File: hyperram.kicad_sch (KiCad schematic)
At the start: 7 parts, among them U2001 IS66WVH16M8DBLL-100B1LI

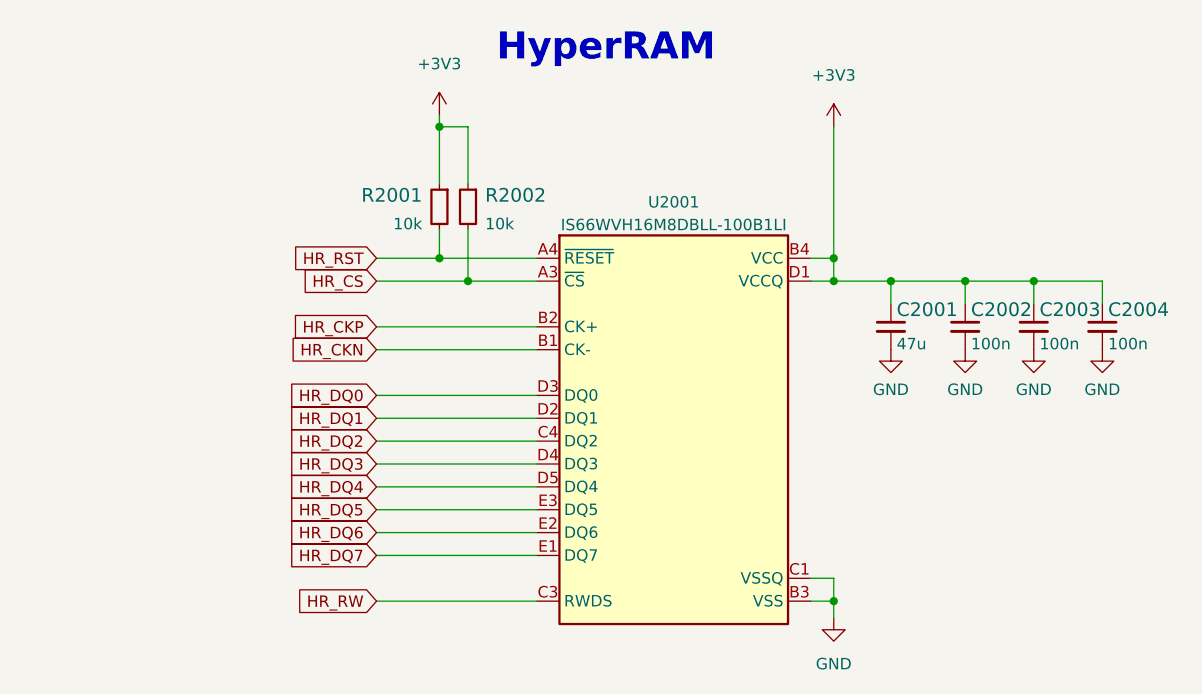
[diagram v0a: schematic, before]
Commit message: Re-annotate schematic
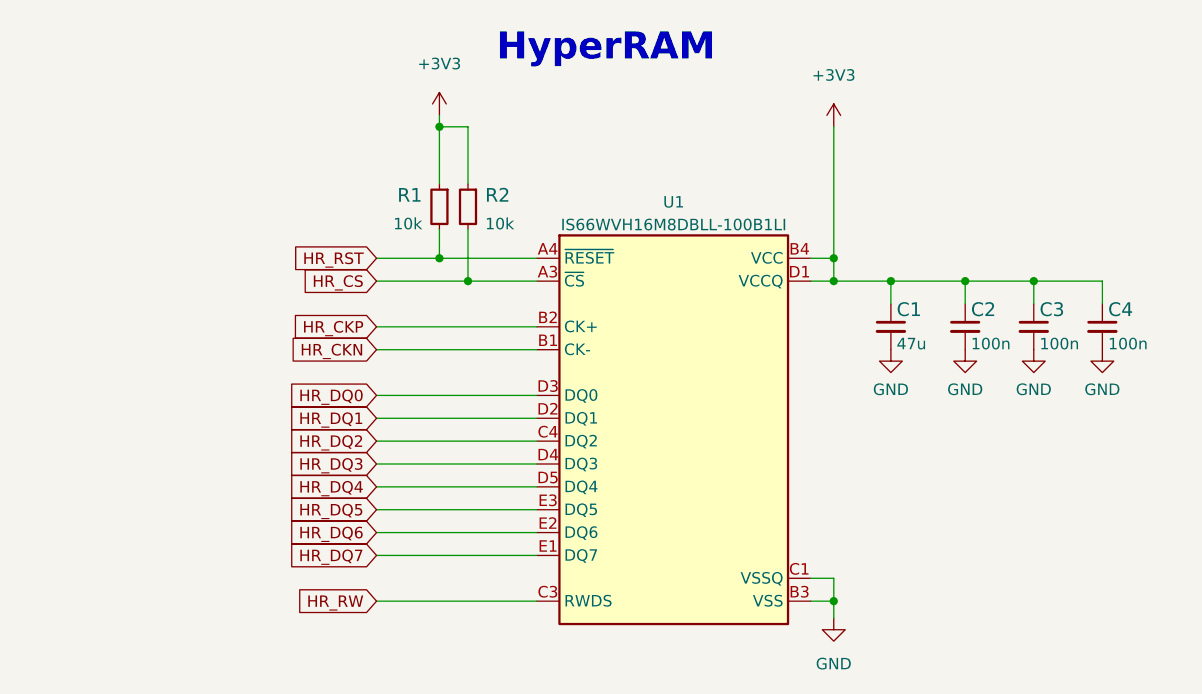
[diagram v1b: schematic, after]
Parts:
- renumbered C2001 to C1, C2002 to C2, C2003 to C3, C2004 to C4, R2001 to R1, R2002 to R2, U2001 to U1
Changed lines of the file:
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@@
   (symbol (lib_id "sodimm-ddr5-tester:C_47u_0603") (at 229.87 131.445 270) (unit 1)
     (in_bom yes) (on_board yes)
-    (property "Reference" "C2001" (id 0) (at 230.505 132.08 90)
+    (property "Reference" "C1" (id 0) (at 230.505 132.08 90)
       (effects (font (size 1.524 1.524)) (justify left))
     )
@@
   (symbol (lib_id "sodimm-ddr5-tester:C_100n_0402") (at 245.745 131.445 270) (unit 1)
     (in_bom yes) (on_board yes)
-    (property "Reference" "C2003" (id 0) (at 246.38 132.08 90)
+    (property "Reference" "C3" (id 0) (at 246.38 132.08 90)
       (effects (font (size 1.524 1.524)) (justify left))
     )
@@
   (symbol (lib_id "sodimm-ddr5-tester:GND") (at 229.87 136.525 0) (unit 1)
     (in_bom yes) (on_board yes) (fields_autoplaced)
-    (property "Reference" "#PWR02002" (id 0) (at 229.87 142.875 0)
+    (property "Reference" "#PWR04" (id 0) (at 229.87 142.875 0)
       (effects (font (size 1.27 1.27)) hide)
     )
@@
   (symbol (lib_id "sodimm-ddr5-tester:R_10k_0402") (at 179.705 118.11 270) (unit 1)
     (in_bom yes) (on_board yes)
-    (property "Reference" "R2001" (id 0) (at 177.8 119.3801 90)
+    (property "Reference" "R1" (id 0) (at 177.8 119.3801 90)
       (effects (font (size 1.524 1.524)) (justify right))
     )
@@
   (symbol (lib_id "sodimm-ddr5-tester:GND") (at 238.125 136.525 0) (unit 1)
     (in_bom yes) (on_board yes) (fields_autoplaced)
-    (property "Reference" "#PWR02003" (id 0) (at 238.125 142.875 0)
+    (property "Reference" "#PWR05" (id 0) (at 238.125 142.875 0)
       (effects (font (size 1.27 1.27)) hide)
     )
@@
   (symbol (lib_id "sodimm-ddr5-tester:GND") (at 245.745 136.525 0) (unit 1)
     (in_bom yes) (on_board yes) (fields_autoplaced)
-    (property "Reference" "#PWR02004" (id 0) (at 245.745 142.875 0)
+    (property "Reference" "#PWR06" (id 0) (at 245.745 142.875 0)
       (effects (font (size 1.27 1.27)) hide)
     )
@@
   (symbol (lib_id "sodimm-ddr5-tester:C_100n_0402") (at 238.125 131.445 270) (unit 1)
     (in_bom yes) (on_board yes)
-    (property "Reference" "C2002" (id 0) (at 238.76 132.08 90)
+    (property "Reference" "C2" (id 0) (at 238.76 132.08 90)
       (effects (font (size 1.524 1.524)) (justify left))
     )
@@
   (symbol (lib_id "sodimm-ddr5-tester:R_10k_0402") (at 182.88 118.11 270) (unit 1)
     (in_bom yes) (on_board yes) (fields_autoplaced)
-    (property "Reference" "R2002" (id 0) (at 184.785 119.38 90)
+    (property "Reference" "R2" (id 0) (at 184.785 119.38 90)
       (effects (font (size 1.524 1.524)) (justify left))
     )
@@
   (symbol (lib_id "sodimm-ddr5-tester:GND") (at 223.52 166.37 0) (unit 1)
     (in_bom yes) (on_board yes) (fields_autoplaced)
-    (property "Reference" "#PWR02001" (id 0) (at 223.52 172.72 0)
+    (property "Reference" "#PWR03" (id 0) (at 223.52 172.72 0)
       (effects (font (size 1.27 1.27)) hide)
     )
@@
   (symbol (lib_id "sodimm-ddr5-tester:C_100n_0402") (at 253.365 131.445 270) (unit 1)
     (in_bom yes) (on_board yes)
-    (property "Reference" "C2004" (id 0) (at 254 132.08 90)
+    (property "Reference" "C4" (id 0) (at 254 132.08 90)
       (effects (font (size 1.524 1.524)) (justify left))
     )
@@
   (symbol (lib_id "sodimm-ddr5-tester:GND") (at 253.365 136.525 0) (unit 1)
     (in_bom yes) (on_board yes) (fields_autoplaced)
-    (property "Reference" "#PWR02005" (id 0) (at 253.365 142.875 0)
+    (property "Reference" "#PWR07" (id 0) (at 253.365 142.875 0)
       (effects (font (size 1.27 1.27)) hide)
     )
@@
   (symbol (lib_id "sodimm-ddr5-tester:+3V3") (at 179.705 110.49 0) (unit 1)
     (in_bom yes) (on_board yes) (fields_autoplaced)
-    (property "Reference" "#PWR0101" (id 0) (at 179.705 114.3 0)
+    (property "Reference" "#PWR01" (id 0) (at 179.705 114.3 0)
       (effects (font (size 1.27 1.27)) hide)
     )
@@
   (symbol (lib_id "sodimm-ddr5-tester:+3V3") (at 223.52 111.76 0) (unit 1)
     (in_bom yes) (on_board yes) (fields_autoplaced)
-    (property "Reference" "#PWR0104" (id 0) (at 223.52 115.57 0)
+    (property "Reference" "#PWR02" (id 0) (at 223.52 115.57 0)
       (effects (font (size 1.27 1.27)) hide)
     )
@@
   (symbol (lib_id "antmicroMemory:IS66WVH16M8DBLL-100B1LI") (at 190.5 126.365 0) (unit 1)
     (in_bom yes) (on_board yes) (fields_autoplaced)
-    (property "Reference" "U2001" (id 0) (at 205.74 120.14 0)
+    (property "Reference" "U1" (id 0) (at 205.74 120.14 0)
       (effects (font (size 1.27 1.27) (thickness 0.15)))
     )

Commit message: Add local libraries
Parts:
- U1: footprint antmicro-footprints:FBGA-25-24_6x8mm_Layout5x5_P1mm -> sodimm-ddr5-tester-footprints:FBGA-25-24_6x8mm_Layout5x5_P1mm; symbol antmicroMemory:IS66WVH16M8DBLL-100B1LI -> sodimm-ddr5-tester:IS66WVH16M8DBLL-100B1LI

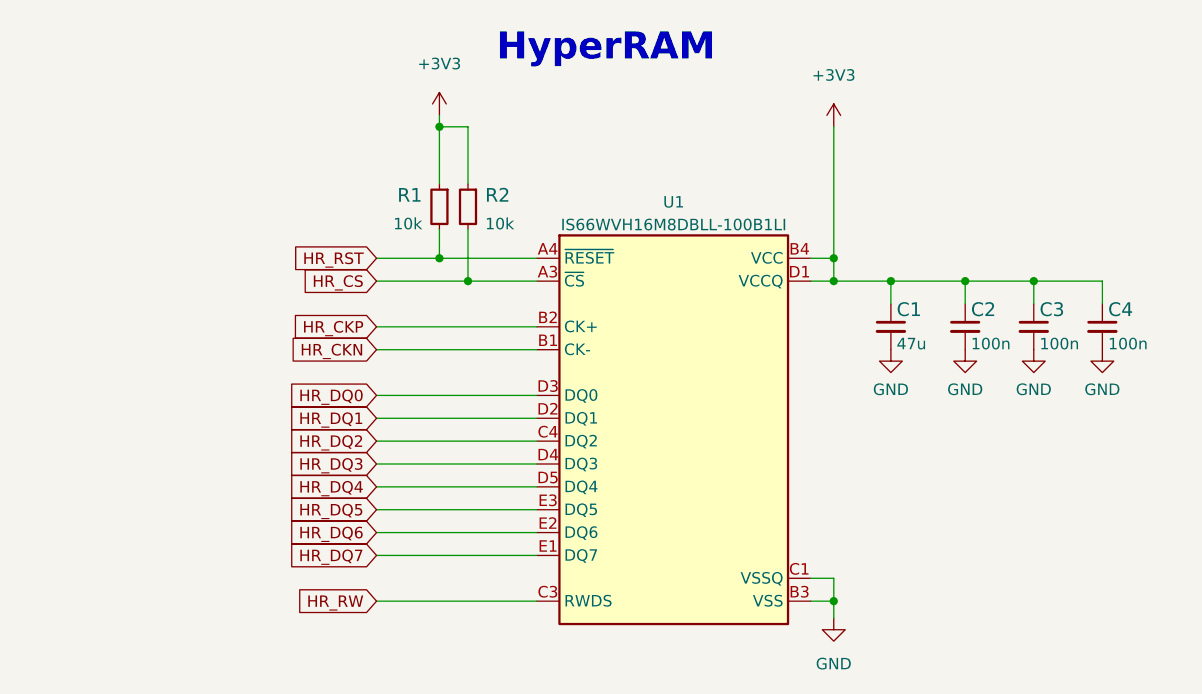
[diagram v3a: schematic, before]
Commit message: Define DDR5, HyperBus and I2C buses. Connect HyperRAM with hierarchical bus
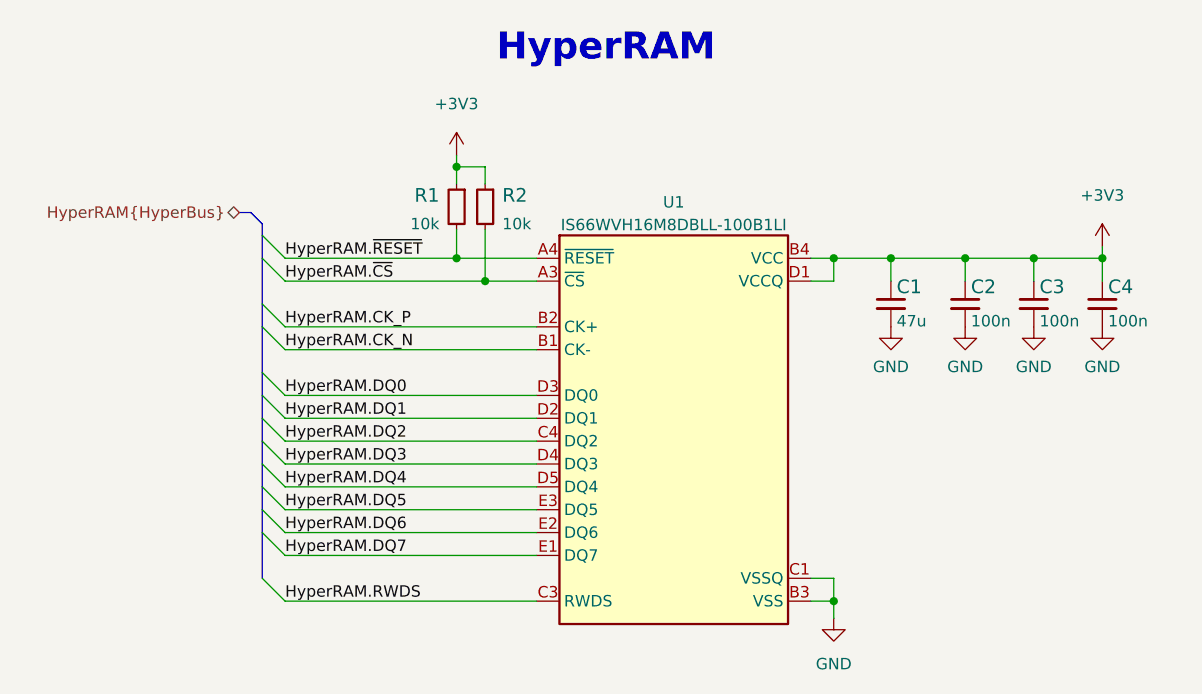
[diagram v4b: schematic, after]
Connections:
- net HR_CKN renamed HyperRAM.CK_N
- net HR_CKP renamed HyperRAM.CK_P
- net HR_CS renamed HyperRAM.~{CS}
- net HR_DQ0 renamed HyperRAM.DQ0
- net HR_DQ1 renamed HyperRAM.DQ1
- net HR_DQ2 renamed HyperRAM.DQ2
- net HR_DQ3 renamed HyperRAM.DQ3
- net HR_DQ4 renamed HyperRAM.DQ4
- net HR_DQ5 renamed HyperRAM.DQ5
- net HR_DQ6 renamed HyperRAM.DQ6
- net HR_DQ7 renamed HyperRAM.DQ7
- net HR_RST renamed HyperRAM.~{RESET}
- net HR_RW renamed HyperRAM.RWDS
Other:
- moved on the sheet: C1, C2, C3, C4, R1, R2

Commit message: Connect DDR hierarchical labels. Define and connect JTAG, RGMII, TDMS, UART, and SDIO buses. Reorganize schematic blocks between sheets
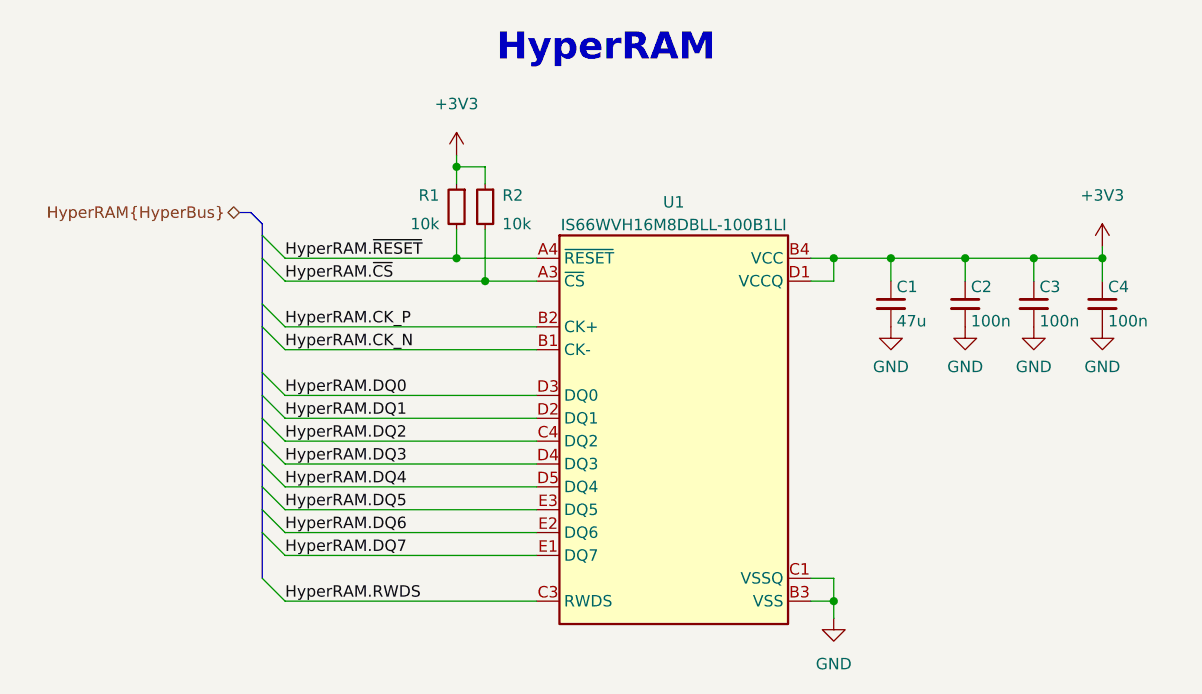
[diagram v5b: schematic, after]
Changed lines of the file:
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@@
     (in_bom yes) (on_board yes)
     (property "Reference" "C1" (id 0) (at 230.505 129.54 90)
-      (effects (font (size 1.524 1.524)) (justify left))
+      (effects (font (size 1.27 1.27)) (justify left))
     )
     (property "Value" "C_47u_0603" (id 1) (at 219.71 149.225 0)
@@
     (in_bom yes) (on_board yes)
     (property "Reference" "C3" (id 0) (at 246.38 129.54 90)
-      (effects (font (size 1.524 1.524)) (justify left))
+      (effects (font (size 1.27 1.27)) (justify left))
     )
     (property "Value" "C_100n_0402" (id 1) (at 235.585 149.225 0)
@@
     (in_bom yes) (on_board yes)
     (property "Reference" "R1" (id 0) (at 179.705 119.3801 90)
-      (effects (font (size 1.524 1.524)) (justify right))
+      (effects (font (size 1.27 1.27)) (justify right))
     )
     (property "Value" "R_10k_0402" (id 1) (at 168.91 138.43 0)
@@
     (in_bom yes) (on_board yes)
     (property "Reference" "C2" (id 0) (at 238.76 129.54 90)
-      (effects (font (size 1.524 1.524)) (justify left))
+      (effects (font (size 1.27 1.27)) (justify left))
     )
     (property "Value" "C_100n_0402" (id 1) (at 227.965 149.225 0)
@@
     (in_bom yes) (on_board yes) (fields_autoplaced)
     (property "Reference" "R2" (id 0) (at 186.69 119.38 90)
-      (effects (font (size 1.524 1.524)) (justify left))
+      (effects (font (size 1.27 1.27)) (justify left))
     )
     (property "Value" "R_10k_0402" (id 1) (at 172.085 138.43 0)
@@
     (in_bom yes) (on_board yes)
     (property "Reference" "C4" (id 0) (at 254 129.54 90)
-      (effects (font (size 1.524 1.524)) (justify left))
+      (effects (font (size 1.27 1.27)) (justify left))
     )
     (property "Value" "C_100n_0402" (id 1) (at 243.205 149.225 0)
